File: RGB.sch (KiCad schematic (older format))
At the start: 10 parts

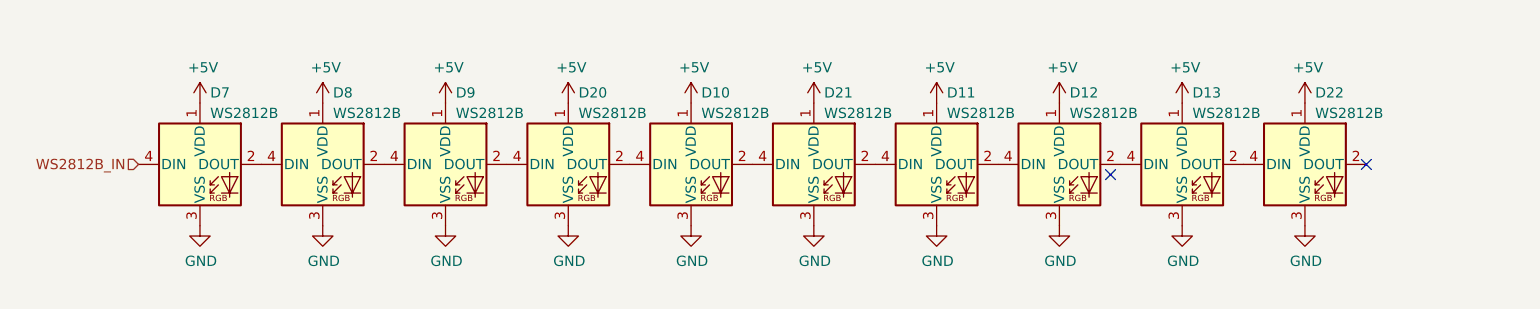
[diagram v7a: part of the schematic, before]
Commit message: Czyszczenie
Usunięto linie 5V oraz 2V8. Poprawiono symbol dla diody RGB
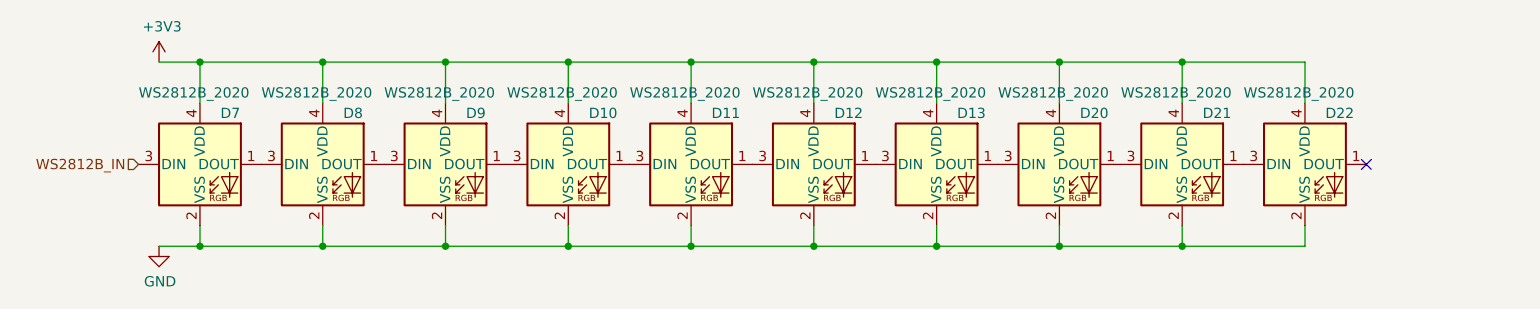
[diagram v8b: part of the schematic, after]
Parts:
- removed D10, D11, D12, D13, D20, D21, D22, D7, D8, D9: WS2812B, WS2812-2020:WS28122020, symbol LED:WS2812B
- added D10, D11, D12, D13, D20, D21, D22, D7, D8, D9: WS2812B_2020, WS2812-2020:WS28122020, symbol synermycha-electronics:WS2812B_2020
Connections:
- net GND: now also D10.2 (VSS), D11.2 (VSS), D12.2 (VSS), D13.2 (VSS), D20.2 (VSS), D21.2 (VSS), D22.2 (VSS), D7.2 (VSS), D8.2 (VSS), D9.2 (VSS)
- net WS2812B_IN: now also D7.3 (DIN)
- new net: D7.1 (DOUT), D8.3 (DIN)
- new net: D8.1 (DOUT), D9.3 (DIN)
- new net: D10.3 (DIN), D9.1 (DOUT)
- new net: D10.1 (DOUT), D11.3 (DIN)
- new net: D11.1 (DOUT), D12.3 (DIN)
- new net: D12.1 (DOUT), D13.3 (DIN)
- new net: D13.1 (DOUT), D20.3 (DIN)
- new net: D21.1 (DOUT), D22.3 (DIN)
- new net: D20.1 (DOUT), D21.3 (DIN)
- new net +3V3: D10.4 (VDD), D11.4 (VDD), D12.4 (VDD), D13.4 (VDD), D20.4 (VDD), D21.4 (VDD), D22.4 (VDD), D7.4 (VDD), D8.4 (VDD), D9.4 (VDD)
- no-connect marks 3 -> 2
